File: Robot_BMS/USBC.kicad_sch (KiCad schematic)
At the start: 9 parts, among them IC2 STUSB4710AQTR, J1 632723300011

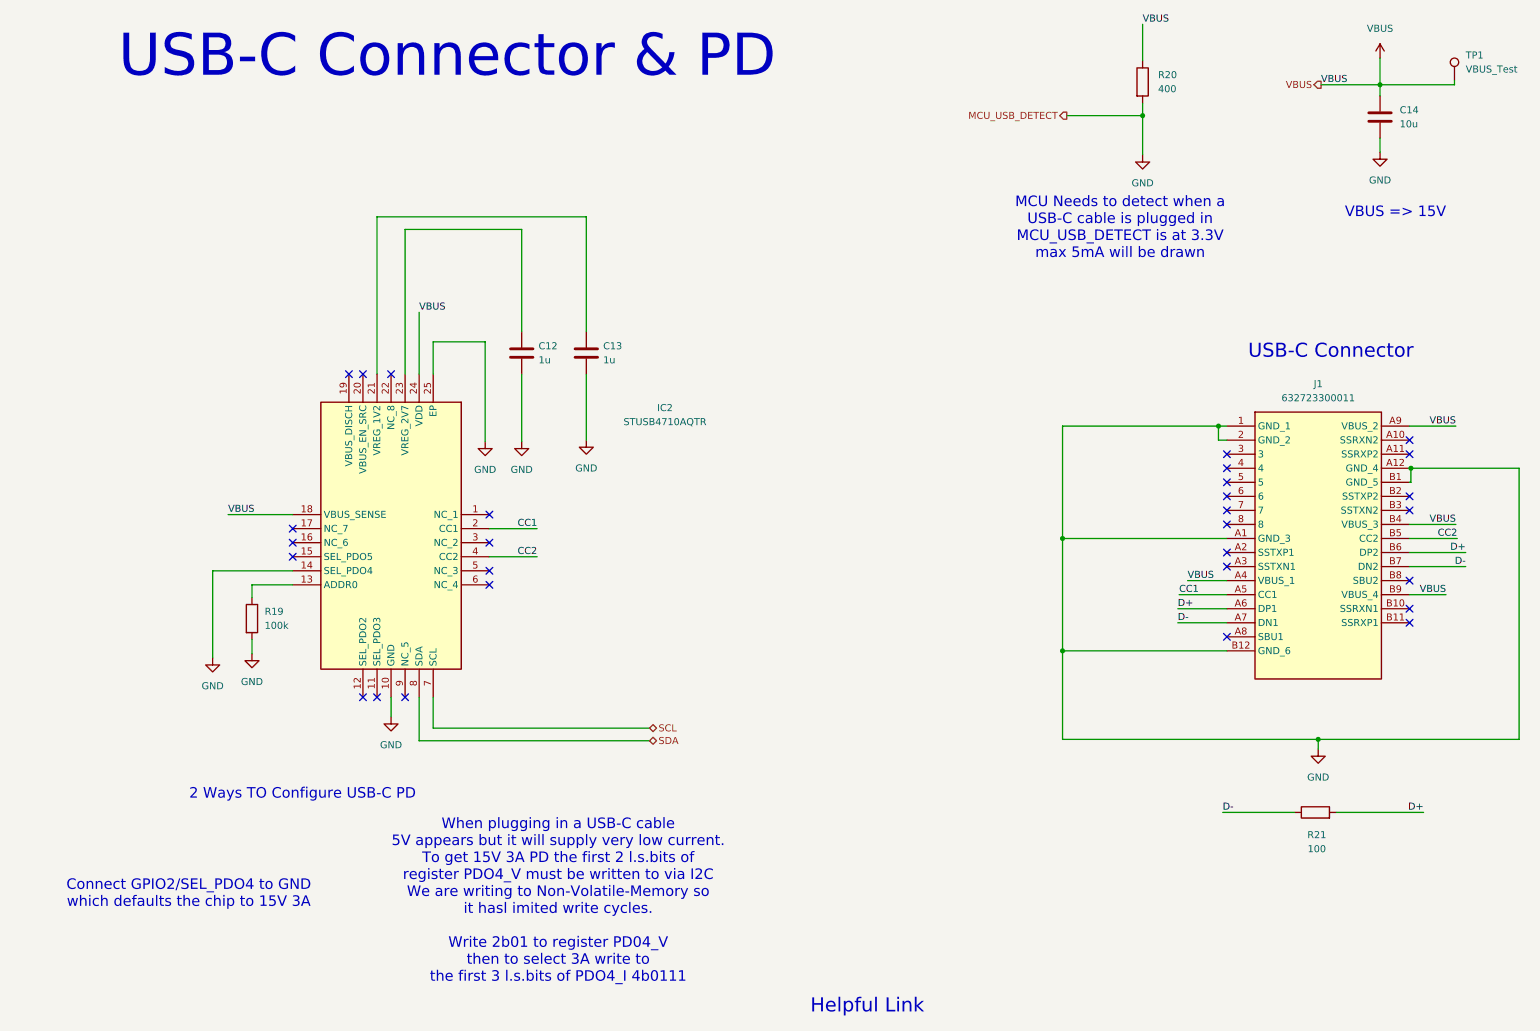
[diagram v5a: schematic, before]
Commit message: System drawing down on top schematic, will start inputting footprints
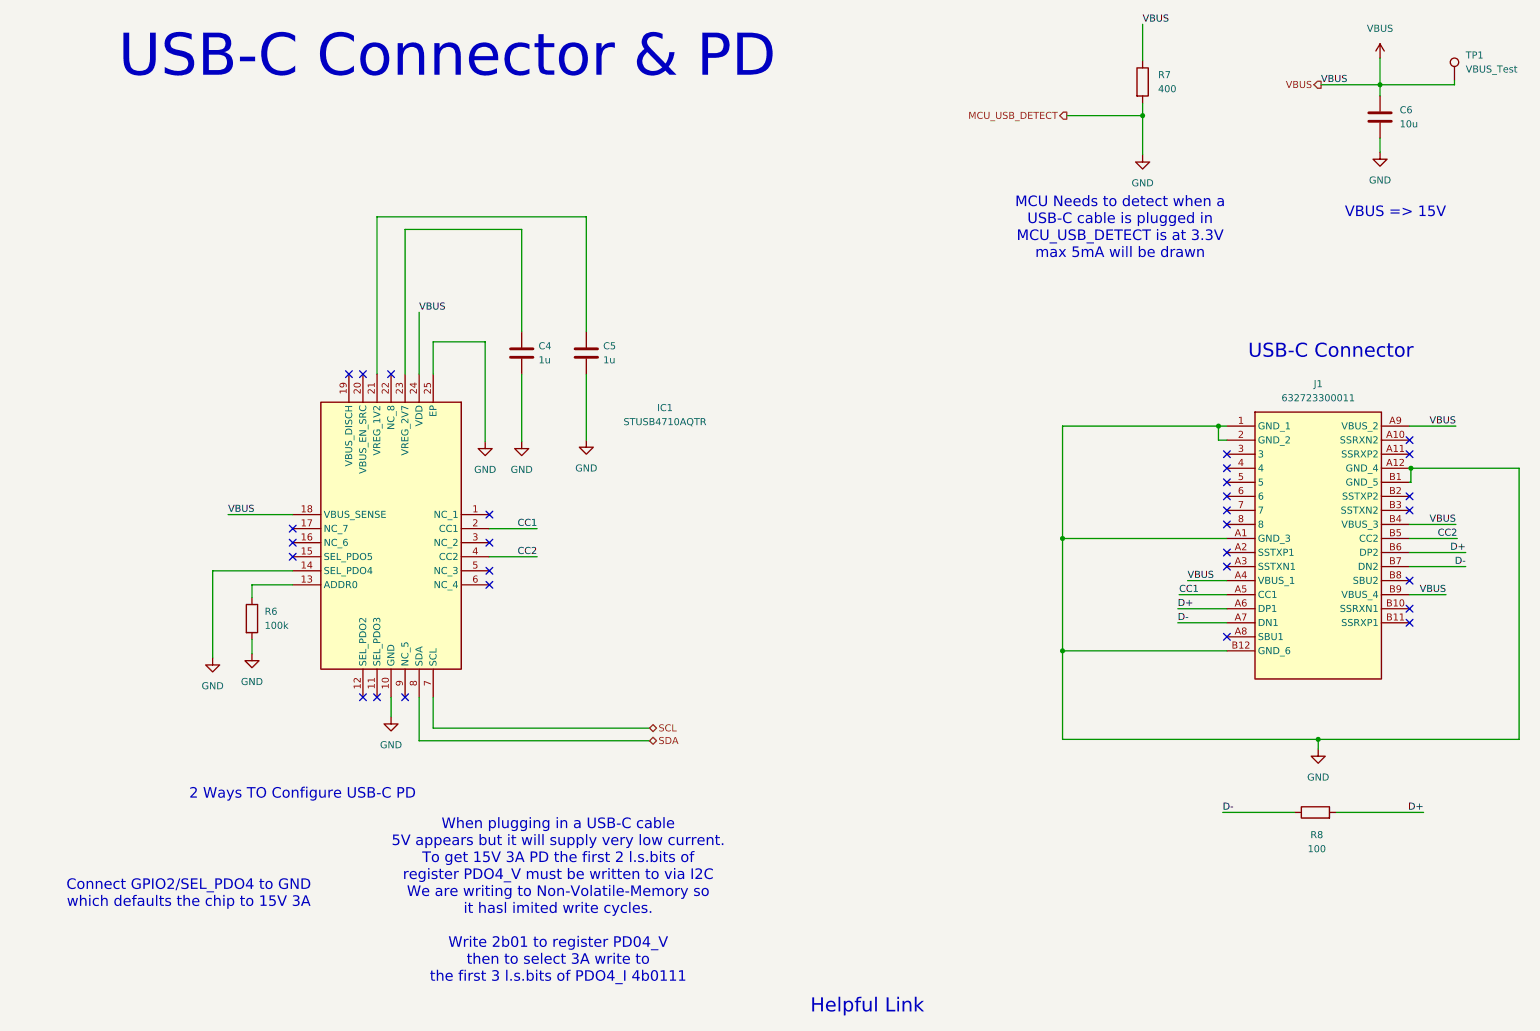
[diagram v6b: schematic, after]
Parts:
- renumbered C12 to C4, C13 to C5, C14 to C6, IC2 to IC1, R19 to R6, R20 to R7, R21 to R8
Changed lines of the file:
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@@
 		(dnp no)
 		(fields_autoplaced yes)
-		(property "Reference" "#PWR017"
+		(property "Reference" "#PWR011"
 			(at 94.234 98.552 0)
 			(effects
@@
 			(project "Robot_BMS"
 				(path "/72551b1c-3d40-4199-8911-e5b015f4abec/c1bdabe1-a4b5-470d-80f8-90d5658c2a45"
-					(reference "#PWR017")
+					(reference "#PWR011")
 					(unit 1)
 				)
@@
 		(dnp no)
 		(fields_autoplaced yes)
-		(property "Reference" "#PWR015"
+		(property "Reference" "#PWR09"
 			(at 52.07 136.906 0)
 			(effects
@@
 			(project "Robot_BMS"
 				(path "/72551b1c-3d40-4199-8911-e5b015f4abec/c1bdabe1-a4b5-470d-80f8-90d5658c2a45"
-					(reference "#PWR015")
+					(reference "#PWR09")
 					(unit 1)
 				)
@@
 		(on_board yes)
 		(dnp no)
-		(property "Reference" "IC2"
+		(property "Reference" "IC1"
 			(at 126.746 86.106 0)
 			(effects
@@
 			(project ""
 				(path "/72551b1c-3d40-4199-8911-e5b015f4abec/c1bdabe1-a4b5-470d-80f8-90d5658c2a45"
-					(reference "IC2")
+					(reference "IC1")
 					(unit 1)
 				)
@@
 		(dnp no)
 		(fields_autoplaced yes)
-		(property "Reference" "#PWR019"
+		(property "Reference" "#PWR013"
 			(at 112.522 98.298 0)
 			(effects
@@
 			(project "Robot_BMS"
 				(path "/72551b1c-3d40-4199-8911-e5b015f4abec/c1bdabe1-a4b5-470d-80f8-90d5658c2a45"
-					(reference "#PWR019")
+					(reference "#PWR013")
 					(unit 1)
 				)
@@
 		(dnp no)
 		(fields_autoplaced yes)
-		(property "Reference" "#PWR014"
+		(property "Reference" "#PWR08"
 			(at 44.958 137.668 0)
 			(effects
@@
 			(project "Robot_BMS"
 				(path "/72551b1c-3d40-4199-8911-e5b015f4abec/c1bdabe1-a4b5-470d-80f8-90d5658c2a45"
-					(reference "#PWR014")
+					(reference "#PWR08")
 					(unit 1)
 				)
@@
 		(dnp no)
 		(fields_autoplaced yes)
-		(property "Reference" "#PWR016"
+		(property "Reference" "#PWR010"
 			(at 77.216 148.336 0)
 			(effects
@@
 			(project "Robot_BMS"
 				(path "/72551b1c-3d40-4199-8911-e5b015f4abec/c1bdabe1-a4b5-470d-80f8-90d5658c2a45"
-					(reference "#PWR016")
+					(reference "#PWR010")
 					(unit 1)
 				)
@@
 		(dnp no)
 		(fields_autoplaced yes)
-		(property "Reference" "C14"
+		(property "Reference" "C6"
 			(at 259.588 32.2579 0)
 			(effects
@@
 			(project "Robot_BMS"
 				(path "/72551b1c-3d40-4199-8911-e5b015f4abec/c1bdabe1-a4b5-470d-80f8-90d5658c2a45"
-					(reference "C14")
+					(reference "C6")
 					(unit 1)
 				)
@@
 		(dnp no)
 		(fields_autoplaced yes)
-		(property "Reference" "#PWR023"
+		(property "Reference" "#PWR017"
 			(at 256.032 46.228 0)
 			(effects
@@
 			(project "Robot_BMS"
 				(path "/72551b1c-3d40-4199-8911-e5b015f4abec/c1bdabe1-a4b5-470d-80f8-90d5658c2a45"
-					(reference "#PWR023")
+					(reference "#PWR017")
 					(unit 1)
 				)
@@
 		(dnp no)
 		(fields_autoplaced yes)
-		(property "Reference" "R20"
+		(property "Reference" "R7"
 			(at 215.9 25.9079 0)
 			(effects
@@
 			(project ""
 				(path "/72551b1c-3d40-4199-8911-e5b015f4abec/c1bdabe1-a4b5-470d-80f8-90d5658c2a45"
-					(reference "R20")
+					(reference "R7")
 					(unit 1)
 				)
@@
 		(dnp no)
 		(fields_autoplaced yes)
-		(property "Reference" "C13"
+		(property "Reference" "C5"
 			(at 115.57 74.9299 0)
 			(effects
@@
 			(project "Robot_BMS"
 				(path "/72551b1c-3d40-4199-8911-e5b015f4abec/c1bdabe1-a4b5-470d-80f8-90d5658c2a45"
-					(reference "C13")
+					(reference "C5")
 					(unit 1)
 				)
@@
 		(dnp no)
 		(fields_autoplaced yes)
-		(property "Reference" "#PWR018"
+		(property "Reference" "#PWR012"
 			(at 100.838 98.552 0)
 			(effects
@@
 			(project "Robot_BMS"
 				(path "/72551b1c-3d40-4199-8911-e5b015f4abec/c1bdabe1-a4b5-470d-80f8-90d5658c2a45"
-					(reference "#PWR018")
+					(reference "#PWR012")
 					(unit 1)
 				)
@@
 		(dnp no)
 		(fields_autoplaced yes)
-		(property "Reference" "R19"
+		(property "Reference" "R6"
 			(at 54.356 122.9359 0)
 			(effects
@@
 			(project ""
 				(path "/72551b1c-3d40-4199-8911-e5b015f4abec/c1bdabe1-a4b5-470d-80f8-90d5658c2a45"
-					(reference "R19")
+					(reference "R6")
 					(unit 1)
 				)
@@
 		(dnp no)
 		(fields_autoplaced yes)
-		(property "Reference" "#PWR021"
+		(property "Reference" "#PWR015"
 			(at 244.856 154.178 0)
 			(effects
@@
 			(project "Robot_BMS"
 				(path "/72551b1c-3d40-4199-8911-e5b015f4abec/c1bdabe1-a4b5-470d-80f8-90d5658c2a45"
-					(reference "#PWR021")
+					(reference "#PWR015")
 					(unit 1)
 				)
@@
 		(dnp no)
 		(fields_autoplaced yes)
-		(property "Reference" "#PWR022"
+		(property "Reference" "#PWR016"
 			(at 256.032 26.67 0)
 			(effects
@@
 			(project ""
 				(path "/72551b1c-3d40-4199-8911-e5b015f4abec/c1bdabe1-a4b5-470d-80f8-90d5658c2a45"
-					(reference "#PWR022")
+					(reference "#PWR016")
 					(unit 1)
 				)
@@
 		(on_board yes)
 		(dnp no)
-		(property "Reference" "R21"
+		(property "Reference" "R8"
 			(at 244.602 163.322 90)
 			(effects
@@
 			(project ""
 				(path "/72551b1c-3d40-4199-8911-e5b015f4abec/c1bdabe1-a4b5-470d-80f8-90d5658c2a45"
-					(reference "R21")
+					(reference "R8")
 					(unit 1)
 				)
@@
 		(dnp no)
 		(fields_autoplaced yes)
-		(property "Reference" "#PWR020"
+		(property "Reference" "#PWR014"
 			(at 213.106 46.736 0)
 			(effects
@@
 			(project "Robot_BMS"
 				(path "/72551b1c-3d40-4199-8911-e5b015f4abec/c1bdabe1-a4b5-470d-80f8-90d5658c2a45"
-					(reference "#PWR020")
+					(reference "#PWR014")
 					(unit 1)
 				)
@@
 		(dnp no)
 		(fields_autoplaced yes)
-		(property "Reference" "C12"
+		(property "Reference" "C4"
 			(at 103.886 74.9299 0)
 			(effects
@@
 			(project ""
 				(path "/72551b1c-3d40-4199-8911-e5b015f4abec/c1bdabe1-a4b5-470d-80f8-90d5658c2a45"
-					(reference "C12")
-					(unit 1)
-				)
+					(reference "C4")
+					(unit 1)
+				)

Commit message: adding footprints and actual passive components
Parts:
- IC1: footprint QFN50P400X400X100-25N-D -> RobotBMS:QFN50P400X400X100-25N-D
- J1: footprint 632723300011 -> RobotBMS:632723300011
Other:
- note added: "All standard Passive componenets are 0603 imperial"
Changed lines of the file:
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@@
+	)
+	(junction
+		(at 256.032 22.86)
+		(diameter 0)
+		(color 0 0 0 0)
 	)
 	(junction
@@
 			(width 0)
 			(type default)
+		)
+	)
+	(text "All standard Passive\ncomponenets are 0603 imperial"
+		(exclude_from_sim no)
+		(at 216.408 172.974 0)
+		(effects
+			(font
+				(size 2.54 2.54)
+			)
 		)
 	)
@@
 			)
 		)
-		(property "Footprint" "QFN50P400X400X100-25N-D"
+		(property "Footprint" "RobotBMS:QFN50P400X400X100-25N-D"
 			(at 63.246 182.55 0)
 			(effects
@@
 			)
 		)
-		(property "Footprint" "632723300011"
+		(property "Footprint" "RobotBMS:632723300011"
 			(at 257.556 184.328 0)
 			(effects
@@
 					(unit 1)
 				)
+			)
+		)
+	)
+	(symbol
+		(lib_id "power:PWR_FLAG")
+		(at 256.032 22.86 270)
+		(unit 1)
+		(exclude_from_sim no)
+		(in_bom yes)
+		(on_board yes)
+		(dnp no)
+		(property "Reference" "#FLG05"
+			(at 257.937 22.86 0)
+			(effects
+				(font
+					(size 1.27 1.27)
+				)
+				(hide yes)
+			)
+		)
+		(property "Value" "PWR_FLAG"
+			(at 263.652 22.86 90)
+			(effects
+				(font
+					(size 1.27 1.27)
+				)
+			)
+		)
+		(property "Footprint" ""
+			(at 256.032 22.86 0)
+			(effects
+				(font
+					(size 1.27 1.27)
+				)
+				(hide yes)
+			)
+		)
+		(property "Datasheet" "~"
+			(at 256.032 22.86 0)
+			(effects
+				(font
+					(size 1.27 1.27)
+				)
+				(hide yes)
+			)
+		)
+		(property "Description" "Special symbol for telling ERC where power comes from"
+			(at 256.032 22.86 0)
+			(effects
+				(font
+					(size 1.27 1.27)
+				)
+				(hide yes)
+			)
+		)
+		(pin "1"
+		)
+		(instances
+			(project "Robot_BMS"
+				(path "/72551b1c-3d40-4199-8911-e5b015f4abec/c1bdabe1-a4b5-470d-80f8-90d5658c2a45"
+					(reference "#FLG05")
+					(unit 1)
+				)

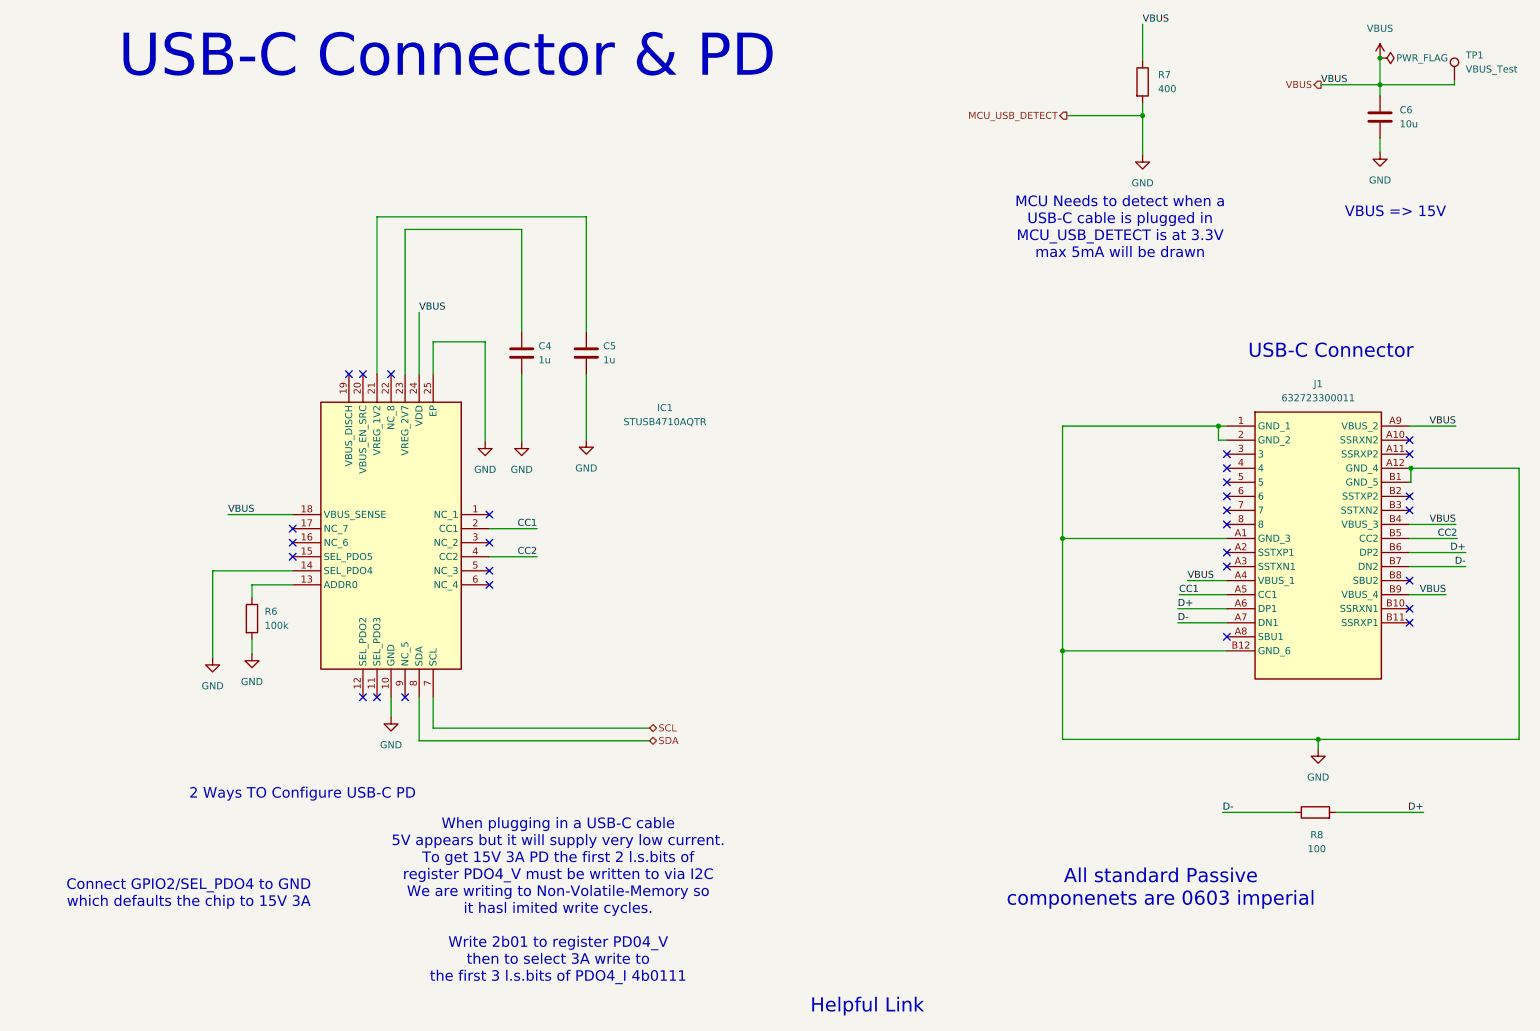
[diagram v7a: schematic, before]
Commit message: still adding in symbols & footprints for passives
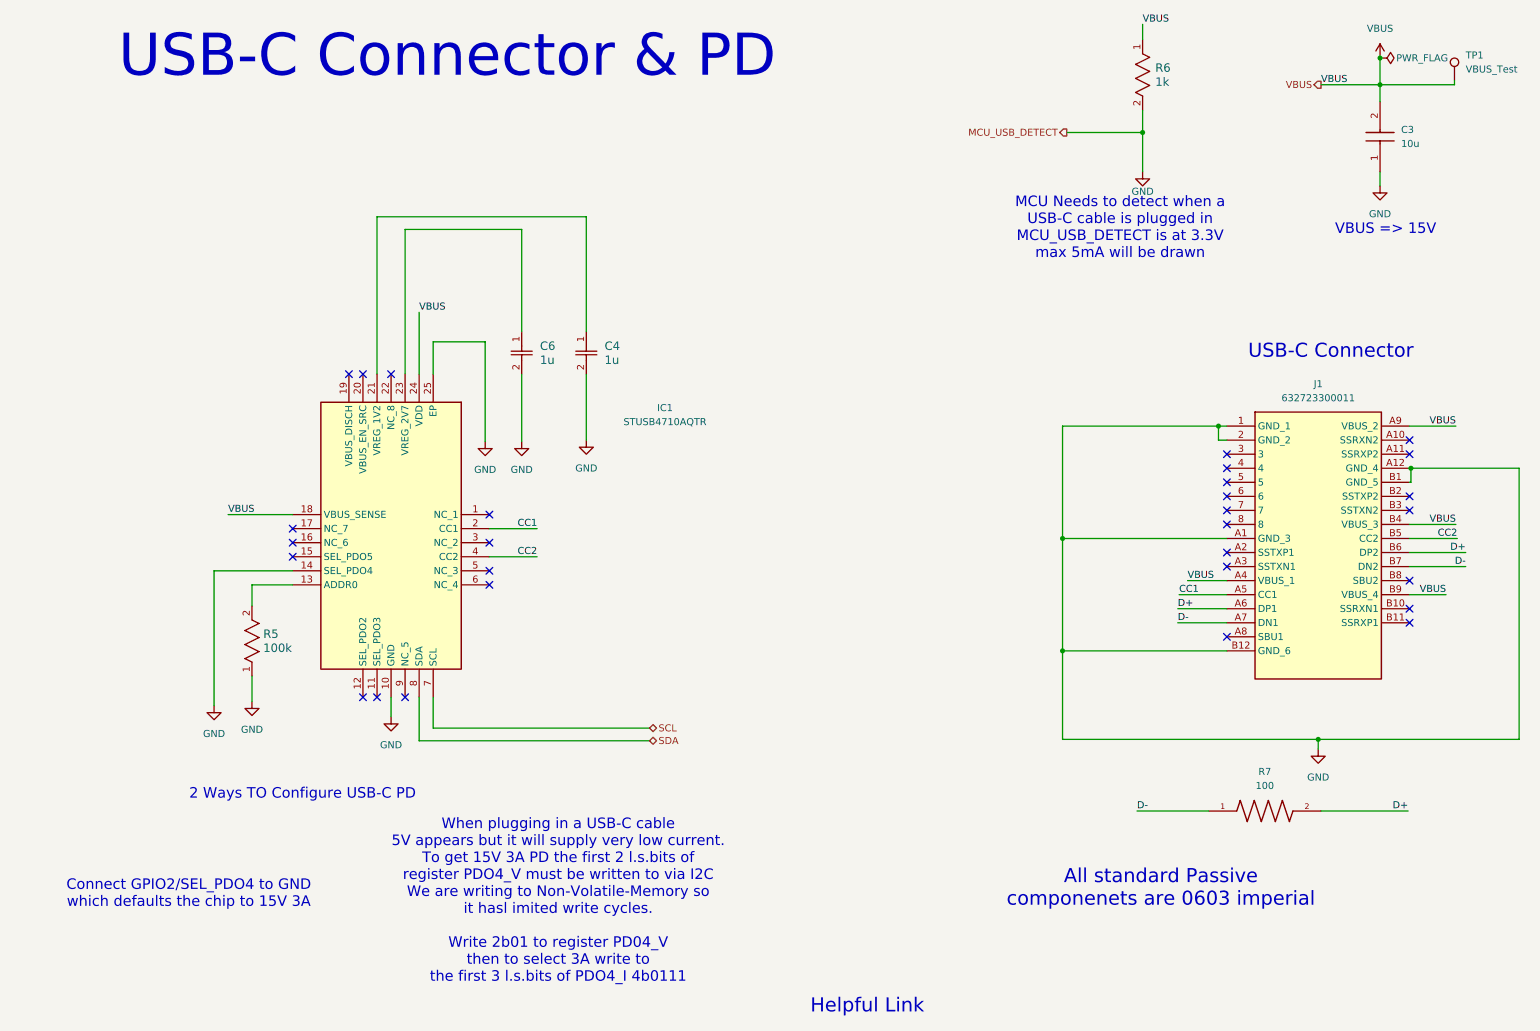
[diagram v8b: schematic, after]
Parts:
- removed C4, C5: 1u, symbol Device:C
- removed C6: 10u, symbol Device:C
- removed R6: 100k, symbol Device:R
- removed R7: 400, symbol Device:R
- removed R8: 100, symbol Device:R
- added C3: 10u, CAPC1608X90N, symbol CL10A106MA8NRNC:CL10A106MA8NRNC
- added C4, C6: 1u, CAP_1608_TDK, symbol C1608X5R1H105K080AB:C1608X5R1H105K080AB
- added R5: 100k, RES_R0603_ROM, symbol ESR03EZPF1003:ESR03EZPF1003
- added R6: 1k, RES_V0603_VIS, symbol CRCW06031K00JNEAIF:CRCW06031K00JNEAIF
- added R7: 100, AT0603DRE07100RL:RESC1608X55N, symbol AT0603DRE07100RL:AT0603DRE07100RL
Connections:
- net D+: now also R7.2
- net D-: now also R7.1
- net GND: now also C3.1, C4.2, C6.2, R5.1, R6.2
- net VBUS: now also C3.2, R6.1
- net at IC1.13 (ADDR0): now also R5.2
- net at IC1.21 (VREG_1V2): now also C4.1
- net at IC1.23 (VREG_2V7): now also C6.1
